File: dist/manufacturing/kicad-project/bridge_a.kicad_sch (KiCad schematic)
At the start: 19 parts, among them J2 B4P-VH(LF)(SN), Q6 CSD19534Q5A, Q7 CSD19534Q5A, Q8 CSD19534Q5A, Q9 CSD19534Q5A

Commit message: Complete orderable PD1180-EPR board release
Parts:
- removed Q6, Q7, Q8, Q9: CSD19534Q5A, symbol Device:U_CSD19534Q5A
- removed RS1: HoLLR2512-3W-33mR-1%, symbol Device:U_HoLLR2512-3W-33mR-1
- removed VMOTOR (x4): VMOTOR, symbol Custom:rail_up
- added Q6: Q6, symbol Custom:CSD19534Q5A_POWER_NMOS
- added Q7: Q7, symbol Custom:CSD19534Q5A_POWER_NMOS
- added Q8: Q8, symbol Custom:CSD19534Q5A_POWER_NMOS
- added Q9: Q9, symbol Custom:CSD19534Q5A_POWER_NMOS
- added R109: 33mΩ, symbol Device:boxresistor_down
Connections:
- net at R38.2: now also Q6.4 (gate); no longer R40.1
- net at R44.1: no longer R42.2
- net at R45.1: no longer R43.2
- net at R44.2: now also Q8.1 (source), Q8.2 (S2), Q8.3 (S3)
- net at R41.1: no longer R39.2
- net at GND.1: now also R109.2
- new net: Q8.4 (gate), R42.2
- new net: Q8.5 (drain), Q8.6 (D2), Q8.7 (D3), Q8.8 (D4), Q8.9 (D5)
- new net: Q6.5 (drain), Q6.6 (D2), Q6.7 (D3), Q6.8 (D4), Q6.9 (D5)
- new net: Q9.4 (gate), R43.2
- new net: Q7.4 (gate), R39.2
- new net: Q7.5 (drain), Q7.6 (D2), Q7.7 (D3), Q7.8 (D4), Q7.9 (D5)
- new net: Q9.5 (drain), Q9.6 (D2), Q9.7 (D3), Q9.8 (D4), Q9.9 (D5)
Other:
- note added: "Q6/Q8: high-side MOSFETs. Q7/Q9: low-side MOSFETs. R109: 33 mOhm, 3 W phase-current shunt."

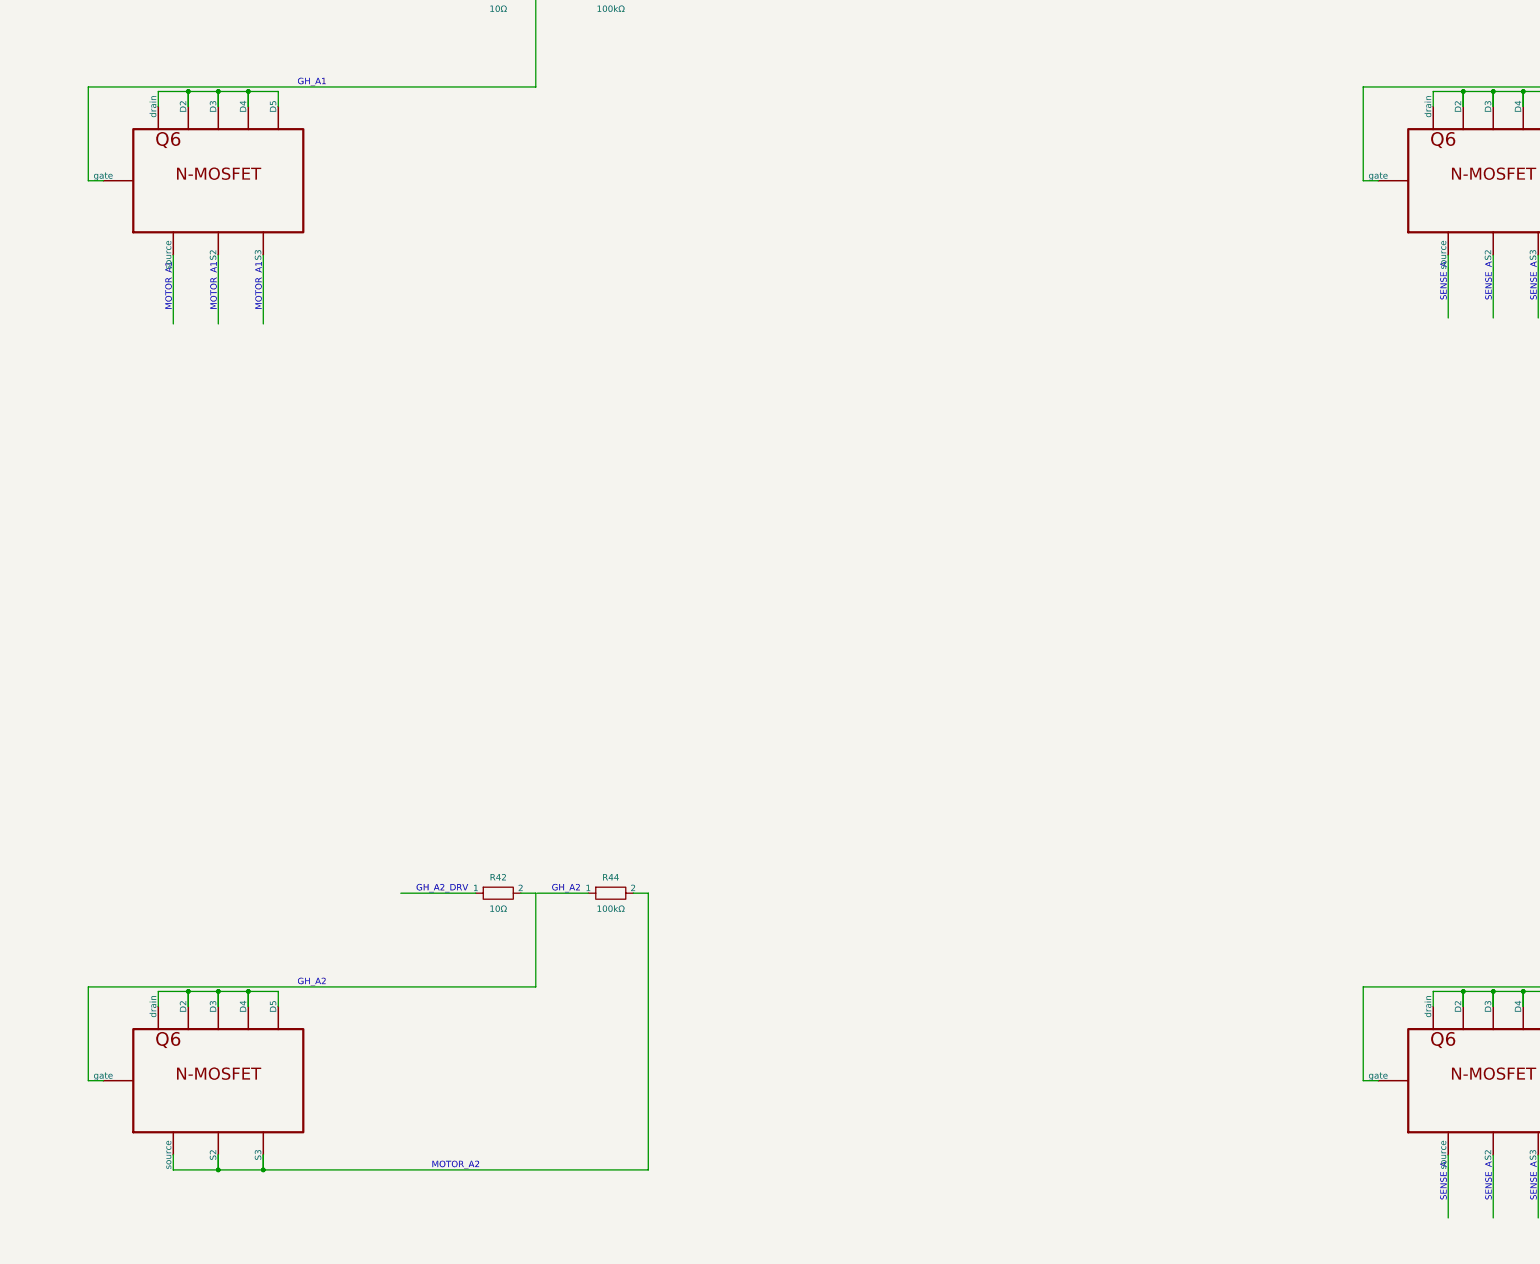
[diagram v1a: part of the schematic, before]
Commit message: Fix schematic style and top-side reset switch
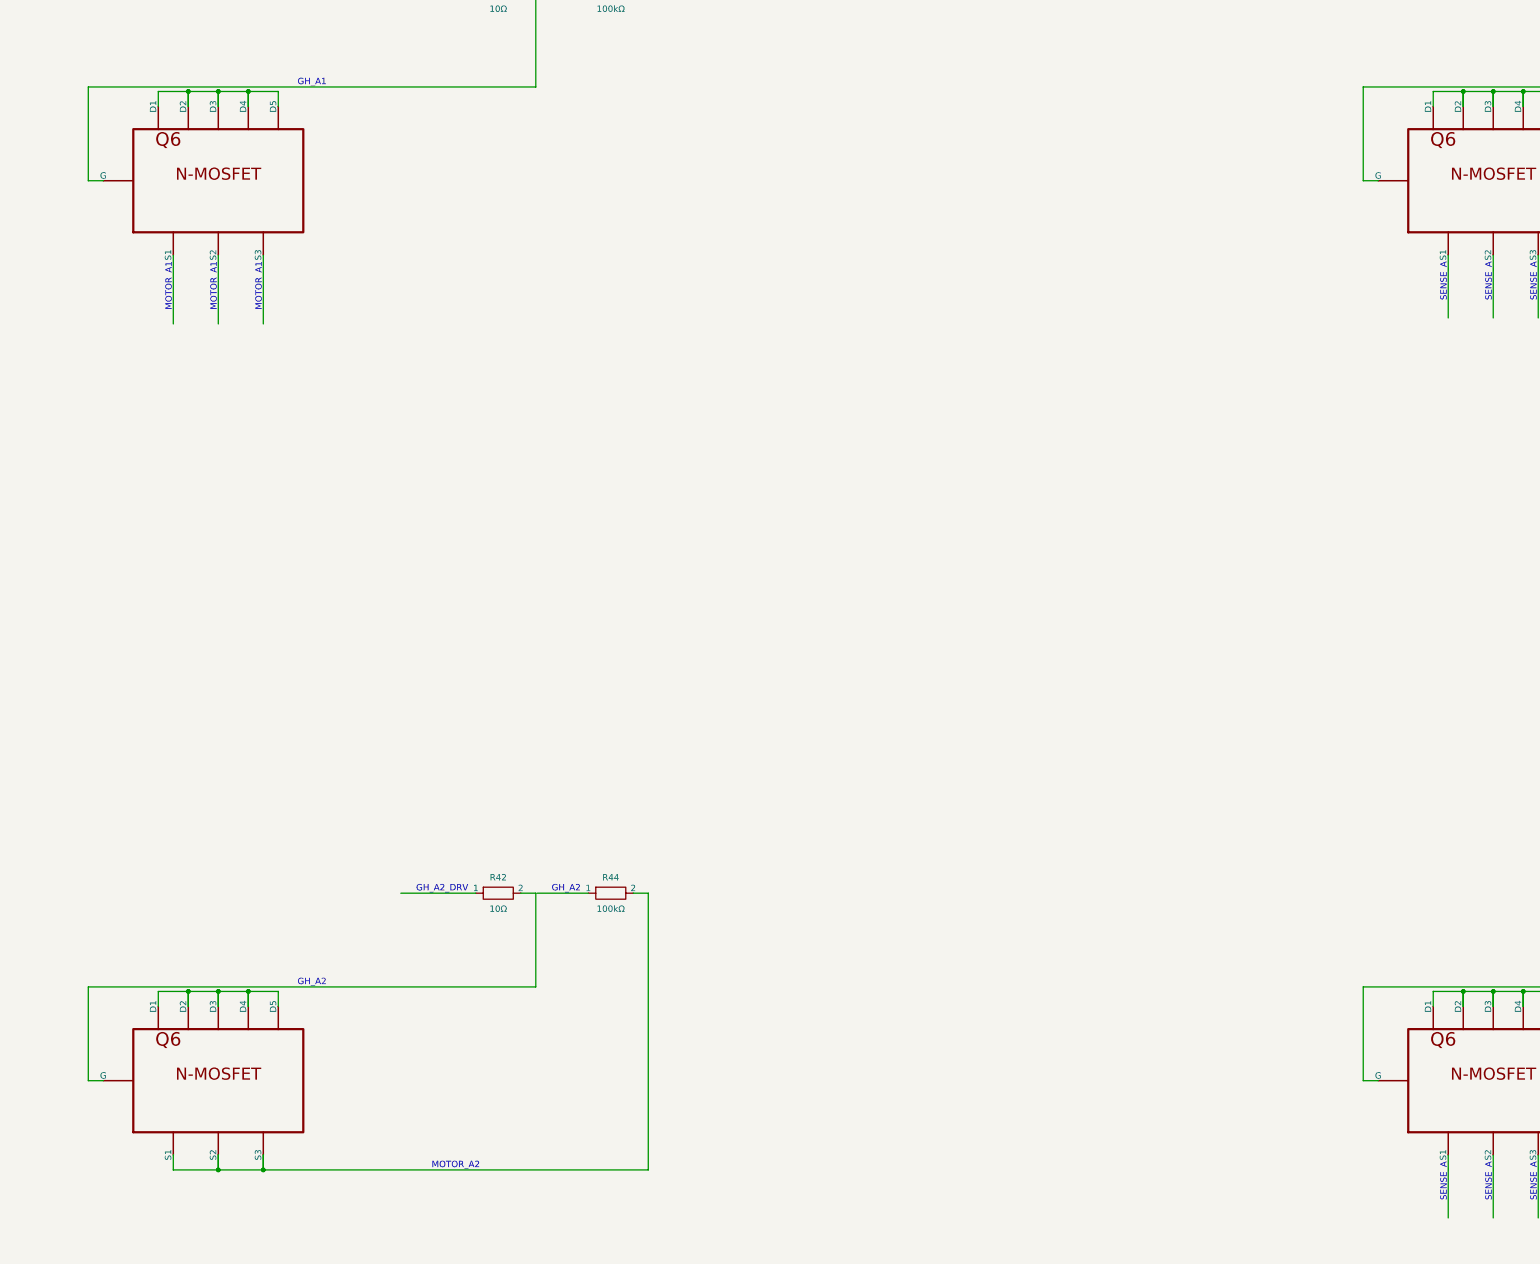
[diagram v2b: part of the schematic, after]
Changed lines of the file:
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@@
     (instances
       (project ""
-        (path "/f5f6ca0d-0209-4855-99b3-5a1edaa43ca4/be5729c3-cf6c-49b5-8c33-8a9b440d376e"
+        (path "/17a83a49-7a29-40ba-a4d1-006f579ceb16/c8415655-c063-4bbf-8145-e2f2fb9d4593"
           (reference "Q6")
           (unit 1)
@@
     (instances
       (project ""
-        (path "/f5f6ca0d-0209-4855-99b3-5a1edaa43ca4/be5729c3-cf6c-49b5-8c33-8a9b440d376e"
+        (path "/17a83a49-7a29-40ba-a4d1-006f579ceb16/c8415655-c063-4bbf-8145-e2f2fb9d4593"
           (reference "Q7")
           (unit 1)
@@
     (instances
       (project ""
-        (path "/f5f6ca0d-0209-4855-99b3-5a1edaa43ca4/be5729c3-cf6c-49b5-8c33-8a9b440d376e"
+        (path "/17a83a49-7a29-40ba-a4d1-006f579ceb16/c8415655-c063-4bbf-8145-e2f2fb9d4593"
           (reference "R38")
           (unit 1)
@@
     (instances
       (project ""
-        (path "/f5f6ca0d-0209-4855-99b3-5a1edaa43ca4/be5729c3-cf6c-49b5-8c33-8a9b440d376e"
+        (path "/17a83a49-7a29-40ba-a4d1-006f579ceb16/c8415655-c063-4bbf-8145-e2f2fb9d4593"
           (reference "R39")
           (unit 1)
@@
     (instances
       (project ""
-        (path "/f5f6ca0d-0209-4855-99b3-5a1edaa43ca4/be5729c3-cf6c-49b5-8c33-8a9b440d376e"
+        (path "/17a83a49-7a29-40ba-a4d1-006f579ceb16/c8415655-c063-4bbf-8145-e2f2fb9d4593"
           (reference "R40")
           (unit 1)
@@
     (instances
       (project ""
-        (path "/f5f6ca0d-0209-4855-99b3-5a1edaa43ca4/be5729c3-cf6c-49b5-8c33-8a9b440d376e"
+        (path "/17a83a49-7a29-40ba-a4d1-006f579ceb16/c8415655-c063-4bbf-8145-e2f2fb9d4593"
           (reference "R41")
           (unit 1)
@@
     (instances
       (project ""
-        (path "/f5f6ca0d-0209-4855-99b3-5a1edaa43ca4/be5729c3-cf6c-49b5-8c33-8a9b440d376e"
+        (path "/17a83a49-7a29-40ba-a4d1-006f579ceb16/c8415655-c063-4bbf-8145-e2f2fb9d4593"
           (reference "Q8")
           (unit 1)
@@
     (instances
       (project ""
-        (path "/f5f6ca0d-0209-4855-99b3-5a1edaa43ca4/be5729c3-cf6c-49b5-8c33-8a9b440d376e"
+        (path "/17a83a49-7a29-40ba-a4d1-006f579ceb16/c8415655-c063-4bbf-8145-e2f2fb9d4593"
           (reference "Q9")
           (unit 1)
@@
     (instances
       (project ""
-        (path "/f5f6ca0d-0209-4855-99b3-5a1edaa43ca4/be5729c3-cf6c-49b5-8c33-8a9b440d376e"
+        (path "/17a83a49-7a29-40ba-a4d1-006f579ceb16/c8415655-c063-4bbf-8145-e2f2fb9d4593"
           (reference "R42")
           (unit 1)
@@
     (instances
       (project ""
-        (path "/f5f6ca0d-0209-4855-99b3-5a1edaa43ca4/be5729c3-cf6c-49b5-8c33-8a9b440d376e"
+        (path "/17a83a49-7a29-40ba-a4d1-006f579ceb16/c8415655-c063-4bbf-8145-e2f2fb9d4593"
           (reference "R43")
           (unit 1)
@@
     (instances
       (project ""
-        (path "/f5f6ca0d-0209-4855-99b3-5a1edaa43ca4/be5729c3-cf6c-49b5-8c33-8a9b440d376e"
+        (path "/17a83a49-7a29-40ba-a4d1-006f579ceb16/c8415655-c063-4bbf-8145-e2f2fb9d4593"
           (reference "R44")
           (unit 1)
@@
     (instances
       (project ""
-        (path "/f5f6ca0d-0209-4855-99b3-5a1edaa43ca4/be5729c3-cf6c-49b5-8c33-8a9b440d376e"
+        (path "/17a83a49-7a29-40ba-a4d1-006f579ceb16/c8415655-c063-4bbf-8145-e2f2fb9d4593"
           (reference "R45")
           (unit 1)
@@
     (instances
       (project ""
-        (path "/f5f6ca0d-0209-4855-99b3-5a1edaa43ca4/be5729c3-cf6c-49b5-8c33-8a9b440d376e"
+        (path "/17a83a49-7a29-40ba-a4d1-006f579ceb16/c8415655-c063-4bbf-8145-e2f2fb9d4593"
           (reference "R109")
           (unit 1)
@@
     (instances
       (project ""
-        (path "/f5f6ca0d-0209-4855-99b3-5a1edaa43ca4/be5729c3-cf6c-49b5-8c33-8a9b440d376e"
+        (path "/17a83a49-7a29-40ba-a4d1-006f579ceb16/c8415655-c063-4bbf-8145-e2f2fb9d4593"
           (reference "J2")
           (unit 1)
@@
     (instances
       (project ""
-        (path "/f5f6ca0d-0209-4855-99b3-5a1edaa43ca4/be5729c3-cf6c-49b5-8c33-8a9b440d376e"
+        (path "/17a83a49-7a29-40ba-a4d1-006f579ceb16/c8415655-c063-4bbf-8145-e2f2fb9d4593"
           (reference "GND")
           (unit 1)

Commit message: fix: finalize single-port EPR controller
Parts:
- removed GND: GND, symbol Custom:rail_down
- J2: value B4P-VH(LF)(SN) -> J2; footprint (none) -> B4P-VH_LF_SN
- Q6, Q7, Q8, Q9: footprint (none) -> CSD19534Q5A
- R109: footprint (none) -> HoLLR2512-3W-33mR-1
- R38, R39, R40, R41, R42, R43, R44, R45: footprint (none) -> resistor_res0603
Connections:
- net GH_A1_DRV: now reaches R38.1
- net GH_A1: now reaches Q6.4 (G), R38.2
- net GH_A1: now also R40.1
- net MOTOR_A1: now reaches Q6.1 (S1)
- net MOTOR_A1: now also J2.1, Q6.2 (S2), Q6.3 (S3), Q7.5 (D1), Q7.6 (D2), Q7.7 (D3), Q7.8 (D4), Q7.9 (D5), R40.2
- net VMOTOR: now reaches Q6.5 (D1), Q6.6 (D2), Q6.7 (D3), Q6.8 (D4), Q6.9 (D5)
- net VMOTOR: now also Q8.5 (D1), Q8.6 (D2), Q8.7 (D3), Q8.8 (D4), Q8.9 (D5)
- net GH_A2: now reaches R44.1
- net GH_A2: now also Q8.4 (G), R42.2
- net MOTOR_A2: now reaches Q8.1 (S1), Q8.2 (S2), Q8.3 (S3), R44.2
- net MOTOR_A2: now also J2.2, Q9.5 (D1), Q9.6 (D2), Q9.7 (D3), Q9.8 (D4), Q9.9 (D5)
- net GND: now reaches R109.2
- net SENSE_A: now reaches Q9.1 (S1)
- net SENSE_A: now also Q7.1 (S1), Q7.2 (S2), Q7.3 (S3), Q9.2 (S2), Q9.3 (S3), R109.1, R41.2, R45.2
- net GL_A2: now reaches Q9.4 (G), R43.2
- net GL_A2: now also R45.1
- net GL_A1_DRV: now reaches R39.1
- net GL_A1: now reaches Q7.4 (G), R39.2
- net GL_A1: now also R41.1
- net GH_A2_DRV: now reaches R42.1
- net MOTOR_B1: now reaches J2.3
- net MOTOR_B2: now reaches J2.4
- net GL_A2_DRV: now reaches R43.1

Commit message: Implement dual USB power/data ECO and consolidate industrial I/O
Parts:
- removed Q6: Q6, CSD19534Q5A, symbol Custom:CSD19534Q5A_POWER_NMOS
- removed Q7: Q7, CSD19534Q5A, symbol Custom:CSD19534Q5A_POWER_NMOS
- removed Q8: Q8, CSD19534Q5A, symbol Custom:CSD19534Q5A_POWER_NMOS
- removed Q9: Q9, CSD19534Q5A, symbol Custom:CSD19534Q5A_POWER_NMOS
- added Q6, Q7, Q8, Q9: CSD19534Q5A, CSD19534Q5A, symbol Device:U_CSD19534Q5A
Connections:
- net GH_A1: now also Q6.4 (G)
- net GH_A2: now also Q8.4 (G)
- net GL_A1: now also Q7.4 (G)
- net GL_A2: now also Q9.4 (G)
- net MOTOR_A1: now also Q6.1 (S1), Q6.2 (S2), Q6.3 (S3), Q7.5 (D1), Q7.6 (D2), Q7.7 (D3), Q7.8 (D4), Q7.9 (D5)
- net MOTOR_A2: now also Q8.1 (S1), Q8.2 (S2), Q8.3 (S3), Q9.5 (D1), Q9.6 (D2), Q9.7 (D3), Q9.8 (D4), Q9.9 (D5)
- net SENSE_A: now also Q7.1 (S1), Q7.2 (S2), Q7.3 (S3), Q9.1 (S1), Q9.2 (S2), Q9.3 (S3)
- net VMOTOR: now also Q6.5 (D1), Q6.6 (D2), Q6.7 (D3), Q6.8 (D4), Q6.9 (D5), Q8.5 (D1), Q8.6 (D2), Q8.7 (D3), Q8.8 (D4), Q8.9 (D5)
